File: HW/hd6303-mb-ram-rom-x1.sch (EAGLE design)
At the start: 28 parts, among them IC2 AM29F010N

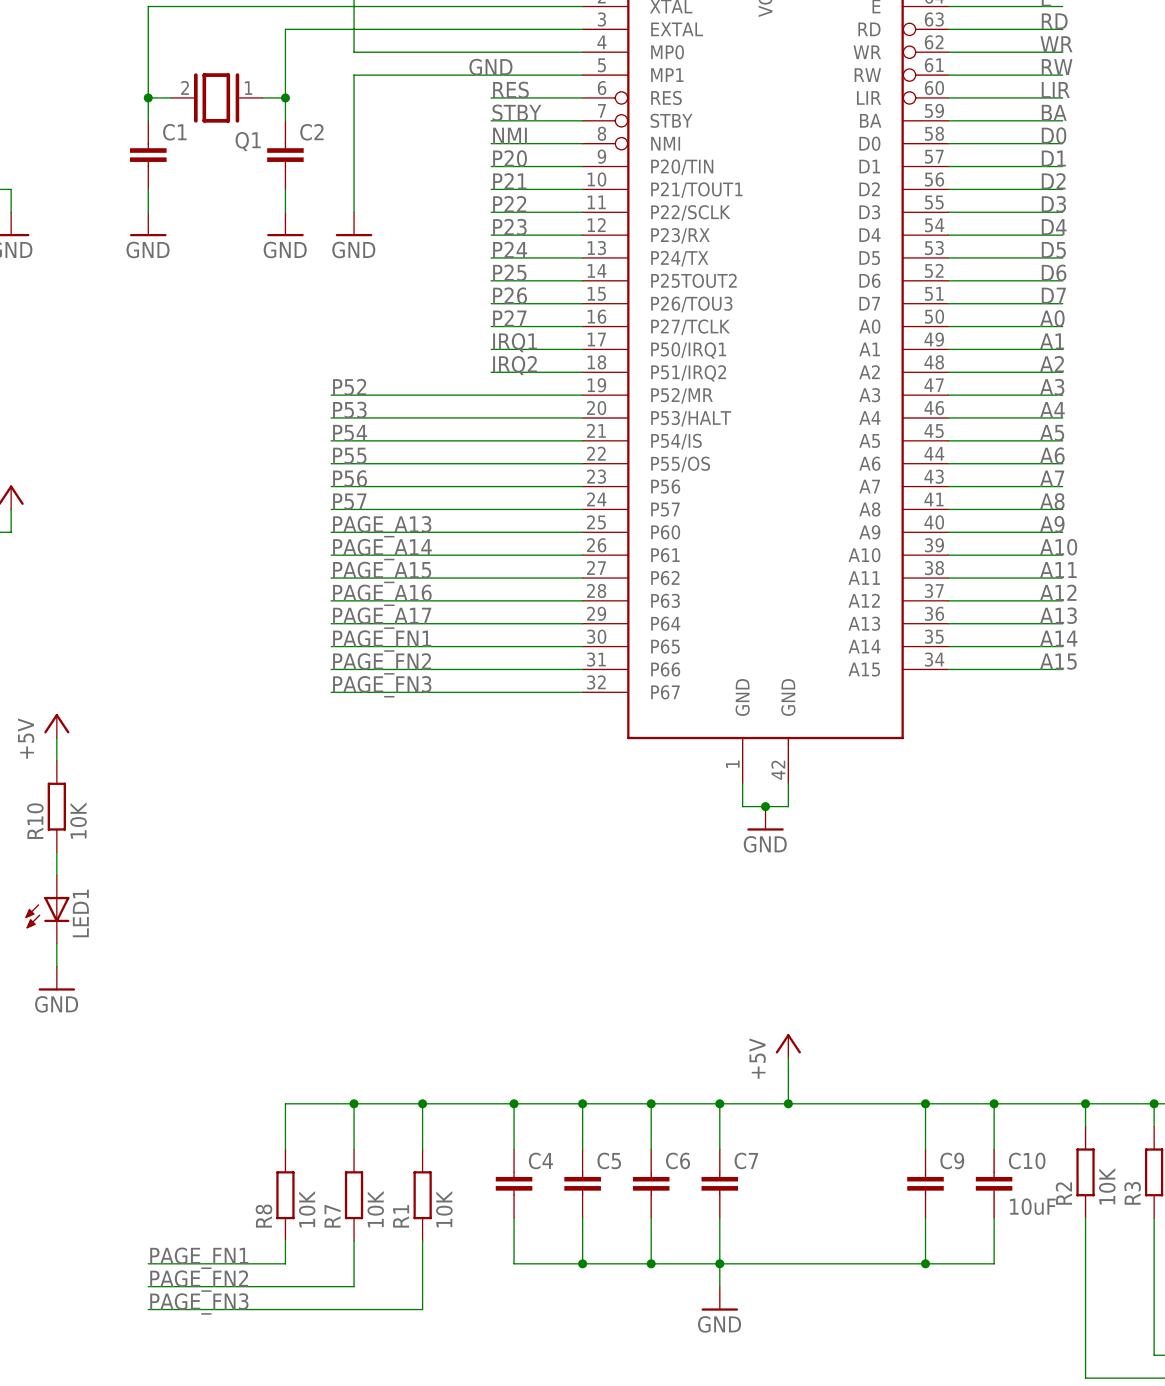
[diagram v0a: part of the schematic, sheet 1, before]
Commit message: pullup for page_a13-page_a17, fixed decoder rom
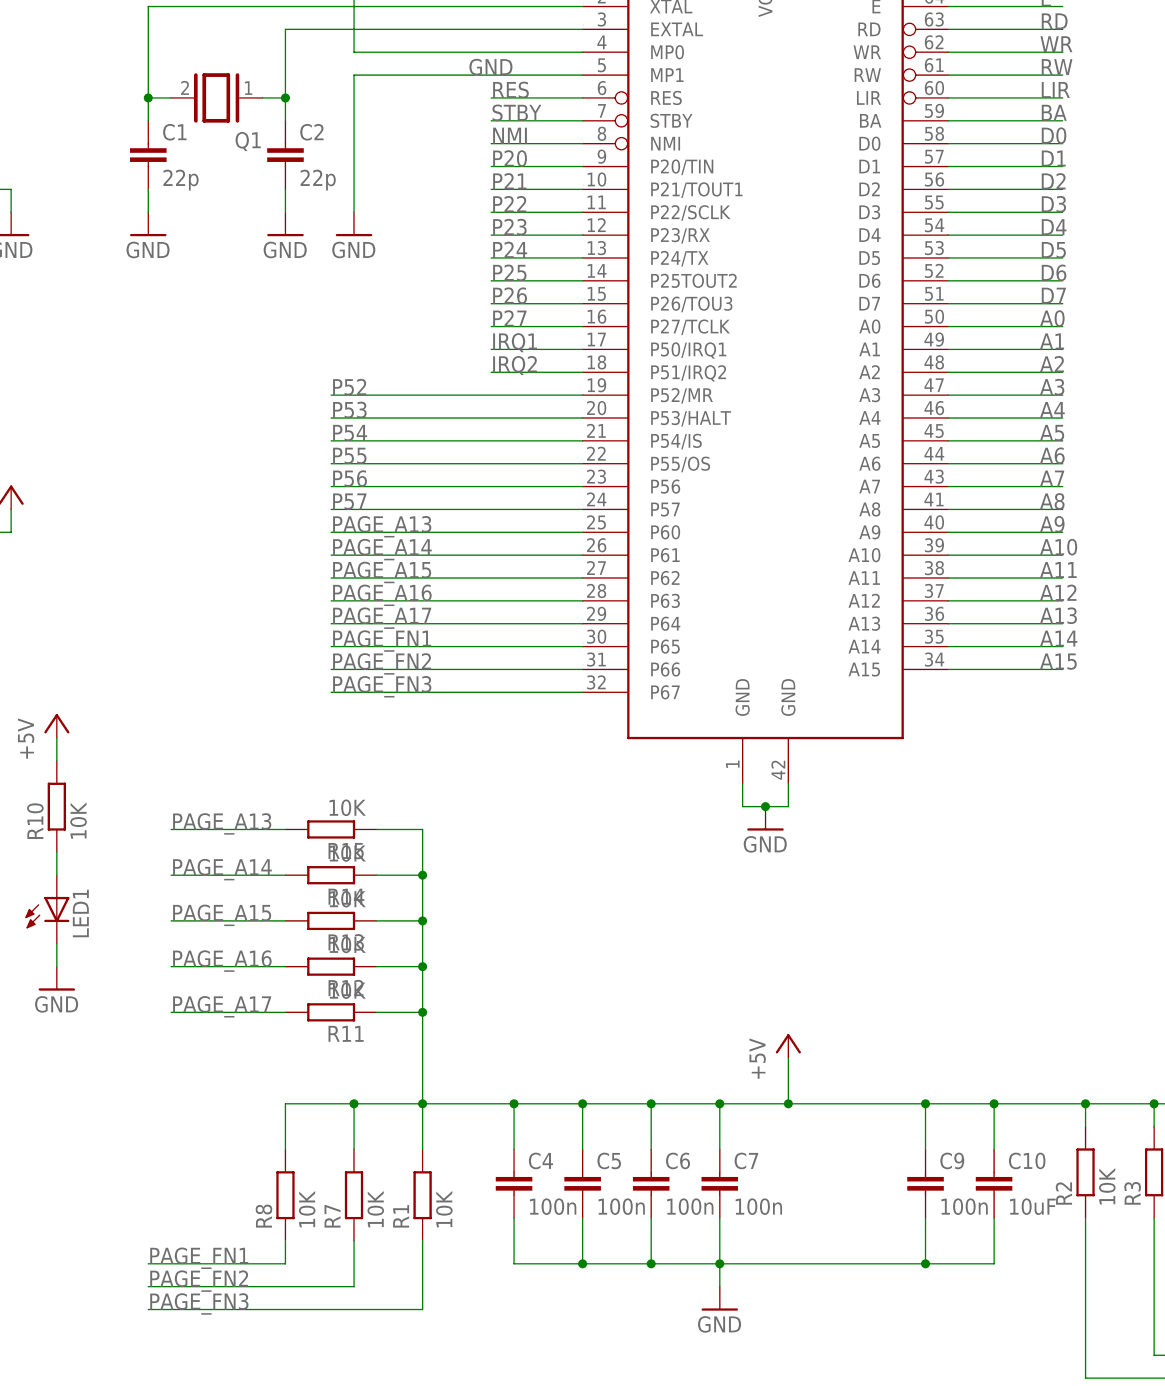
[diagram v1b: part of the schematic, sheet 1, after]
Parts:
- added R11, R12, R13, R14, R15: 10K, resistor:R-EU_R0603
- C1, C2: value (none) -> 22p
- C4, C5, C6, C7, C9: value (none) -> 100n
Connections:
- net +5V: now also R11.1, R12.1, R13.1, R14.1, R15.1
- net PAGE_A13: now also R15.2
- net PAGE_A14: now also R14.2
- net PAGE_A15: now also R13.2
- net PAGE_A16: now also R12.2
- net PAGE_A17: now also R11.2
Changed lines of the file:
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@@
 <part name="GND1" library="supply1" library_urn="urn:adsk.eagle:library:371" deviceset="GND" device=""/>
 <part name="Q1" library="special" deviceset="XTAL/S" device=""/>
-<part name="C1" library="rcl" library_urn="urn:adsk.eagle:library:334" deviceset="C-EU" device="C0603" package3d_urn="urn:adsk.eagle:package:23616/2"/>
-<part name="C2" library="rcl" deviceset="C-EU" device="C0603"/>
+<part name="C1" library="rcl" library_urn="urn:adsk.eagle:library:334" deviceset="C-EU" device="C0603" package3d_urn="urn:adsk.eagle:package:23616/2" value="22p"/>
+<part name="C2" library="rcl" deviceset="C-EU" device="C0603" value="22p"/>
 <part name="GND8" library="supply1" deviceset="GND" device=""/>
 <part name="GND9" library="supply1" deviceset="GND" device=""/>
@@
 <part name="GND4" library="supply1" library_urn="urn:adsk.eagle:library:371" deviceset="GND" device=""/>
 <part name="P+3" library="supply1" library_urn="urn:adsk.eagle:library:371" deviceset="+5V" device=""/>
-<part name="C4" library="rcl" deviceset="C-EU" device="C0603"/>
-<part name="C5" library="rcl" deviceset="C-EU" device="C0603"/>
-<part name="C6" library="rcl" deviceset="C-EU" device="C0603"/>
-<part name="C7" library="rcl" deviceset="C-EU" device="C0603"/>
-<part name="C9" library="rcl" deviceset="C-EU" device="C0603"/>
+<part name="C4" library="rcl" deviceset="C-EU" device="C0603" value="100n"/>
+<part name="C5" library="rcl" deviceset="C-EU" device="C0603" value="100n"/>
+<part name="C6" library="rcl" deviceset="C-EU" device="C0603" value="100n"/>
+<part name="C7" library="rcl" deviceset="C-EU" device="C0603" value="100n"/>
+<part name="C9" library="rcl" deviceset="C-EU" device="C0603" value="100n"/>
 <part name="GND16" library="supply1" library_urn="urn:adsk.eagle:library:371" deviceset="GND" device=""/>
 <part name="C10" library="resistor" library_urn="urn:adsk.eagle:library:348" deviceset="C-EU" device="C0805" package3d_urn="urn:adsk.eagle:package:26137/1" value="10uF"/>
@@
 <part name="LED1" library="led" library_urn="urn:adsk.eagle:library:259" deviceset="LED" device="5MM" package3d_urn="urn:adsk.eagle:package:15799/2"/>
 <part name="GND2" library="supply1" library_urn="urn:adsk.eagle:library:371" deviceset="GND" device=""/>
+<part name="R11" library="resistor" library_urn="urn:adsk.eagle:library:348" deviceset="R-EU_" device="R0603" package3d_urn="urn:adsk.eagle:package:26057/1" value="10K"/>
+<part name="R12" library="resistor" library_urn="urn:adsk.eagle:library:348" deviceset="R-EU_" device="R0603" package3d_urn="urn:adsk.eagle:package:26057/1" value="10K"/>
+<part name="R13" library="resistor" library_urn="urn:adsk.eagle:library:348" deviceset="R-EU_" device="R0603" package3d_urn="urn:adsk.eagle:package:26057/1" value="10K"/>
+<part name="R14" library="resistor" library_urn="urn:adsk.eagle:library:348" deviceset="R-EU_" device="R0603" package3d_urn="urn:adsk.eagle:package:26057/1" value="10K"/>
+<part name="R15" library="resistor" library_urn="urn:adsk.eagle:library:348" deviceset="R-EU_" device="R0603" package3d_urn="urn:adsk.eagle:package:26057/1" value="10K"/>
 </parts>
 <sheets>
@@
 <instance part="GND2" gate="1" x="48.26" y="27.94" smashed="yes">
 <attribute name="VALUE" x="45.72" y="25.4" size="1.778" layer="96"/>
+</instance>
+<instance part="R11" gate="G$1" x="78.74" y="25.4" smashed="yes" rot="R180">
+<attribute name="NAME" x="82.55" y="23.9014" size="1.778" layer="95" rot="R180"/>
+<attribute name="VALUE" x="82.55" y="28.702" size="1.778" layer="96" rot="R180"/>
+</instance>
+<instance part="R12" gate="G$1" x="78.74" y="30.48" smashed="yes" rot="R180">
+<attribute name="NAME" x="82.55" y="28.9814" size="1.778" layer="95" rot="R180"/>
+<attribute name="VALUE" x="82.55" y="33.782" size="1.778" layer="96" rot="R180"/>
+</instance>
+<instance part="R13" gate="G$1" x="78.74" y="35.56" smashed="yes" rot="R180">
+<attribute name="NAME" x="82.55" y="34.0614" size="1.778" layer="95" rot="R180"/>
+<attribute name="VALUE" x="82.55" y="38.862" size="1.778" layer="96" rot="R180"/>
+</instance>
+<instance part="R14" gate="G$1" x="78.74" y="40.64" smashed="yes" rot="R180">
+<attribute name="NAME" x="82.55" y="39.1414" size="1.778" layer="95" rot="R180"/>
+<attribute name="VALUE" x="82.55" y="43.942" size="1.778" layer="96" rot="R180"/>
+</instance>
+<instance part="R15" gate="G$1" x="78.74" y="45.72" smashed="yes" rot="R180">
+<attribute name="NAME" x="82.55" y="44.2214" size="1.778" layer="95" rot="R180"/>
+<attribute name="VALUE" x="82.55" y="49.022" size="1.778" layer="96" rot="R180"/>
 </instance>
 </instances>
@@
 <wire x1="200.66" y1="15.24" x2="200.66" y2="12.7" width="0.1524" layer="91"/>
 <junction x="193.04" y="15.24"/>
+<pinref part="R15" gate="G$1" pin="1"/>
+<wire x1="83.82" y1="45.72" x2="88.9" y2="45.72" width="0.1524" layer="91"/>
+<wire x1="88.9" y1="45.72" x2="88.9" y2="40.64" width="0.1524" layer="91"/>
+<pinref part="R14" gate="G$1" pin="1"/>
+<wire x1="88.9" y1="40.64" x2="88.9" y2="35.56" width="0.1524" layer="91"/>
+<wire x1="88.9" y1="35.56" x2="88.9" y2="30.48" width="0.1524" layer="91"/>
+<wire x1="88.9" y1="30.48" x2="88.9" y2="25.4" width="0.1524" layer="91"/>
+<wire x1="88.9" y1="25.4" x2="88.9" y2="15.24" width="0.1524" layer="91"/>
+<wire x1="83.82" y1="40.64" x2="88.9" y2="40.64" width="0.1524" layer="91"/>
+<junction x="88.9" y="40.64"/>
+<pinref part="R13" gate="G$1" pin="1"/>
+<wire x1="83.82" y1="35.56" x2="88.9" y2="35.56" width="0.1524" layer="91"/>
+<junction x="88.9" y="35.56"/>
+<pinref part="R12" gate="G$1" pin="1"/>
+<wire x1="83.82" y1="30.48" x2="88.9" y2="30.48" width="0.1524" layer="91"/>
+<junction x="88.9" y="30.48"/>
+<pinref part="R11" gate="G$1" pin="1"/>
+<wire x1="83.82" y1="25.4" x2="88.9" y2="25.4" width="0.1524" layer="91"/>
+<junction x="88.9" y="25.4"/>
 </segment>
 <segment>
@@
 <label x="243.84" y="30.48" size="1.778" layer="95"/>
 </segment>
+<segment>
+<pinref part="R11" gate="G$1" pin="2"/>
+<wire x1="73.66" y1="25.4" x2="60.96" y2="25.4" width="0.1524" layer="91"/>
+<label x="60.96" y="25.4" size="1.778" layer="95"/>
+</segment>
 </net>
 <net name="PAGE_A13" class="0">
@@
 <label x="243.84" y="40.64" size="1.778" layer="95"/>
 </segment>
+<segment>
+<pinref part="R15" gate="G$1" pin="2"/>
+<wire x1="73.66" y1="45.72" x2="60.96" y2="45.72" width="0.1524" layer="91"/>
+<label x="60.96" y="45.72" size="1.778" layer="95"/>
+</segment>
 </net>
 <net name="PAGE_A14" class="0">
@@
 <label x="243.84" y="38.1" size="1.778" layer="95"/>
 </segment>
+<segment>
+<pinref part="R14" gate="G$1" pin="2"/>
+<wire x1="73.66" y1="40.64" x2="60.96" y2="40.64" width="0.1524" layer="91"/>
+<label x="60.96" y="40.64" size="1.778" layer="95"/>
+</segment>
 </net>
 <net name="PAGE_A15" class="0">
@@
 <label x="243.84" y="35.56" size="1.778" layer="95"/>
 </segment>
+<segment>
+<pinref part="R13" gate="G$1" pin="2"/>
+<wire x1="73.66" y1="35.56" x2="60.96" y2="35.56" width="0.1524" layer="91"/>
+<label x="60.96" y="35.56" size="1.778" layer="95"/>
+</segment>
 </net>
 <net name="PAGE_A16" class="0">
@@
 <label x="243.84" y="33.02" size="1.778" layer="95"/>
 </segment>
-</net>
+<segment>
+<pinref part="R12" gate="G$1" pin="2"/>
+<wire x1="73.66" y1="30.48" x2="60.96" y2="30.48" width="0.1524" layer="91"/>
+<label x="60.96" y="30.48" size="1.778" layer="95"/>
+</segment>
+</net>
